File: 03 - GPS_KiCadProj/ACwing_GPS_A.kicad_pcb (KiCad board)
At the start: 2 copper layers, 30 x 30 mm, 28 parts, among them J1 Qwiic IN, J2 Qwiic OUT, Q1 2N7002, U1 SAM-M10Q-00B, U3 IIS2MDC

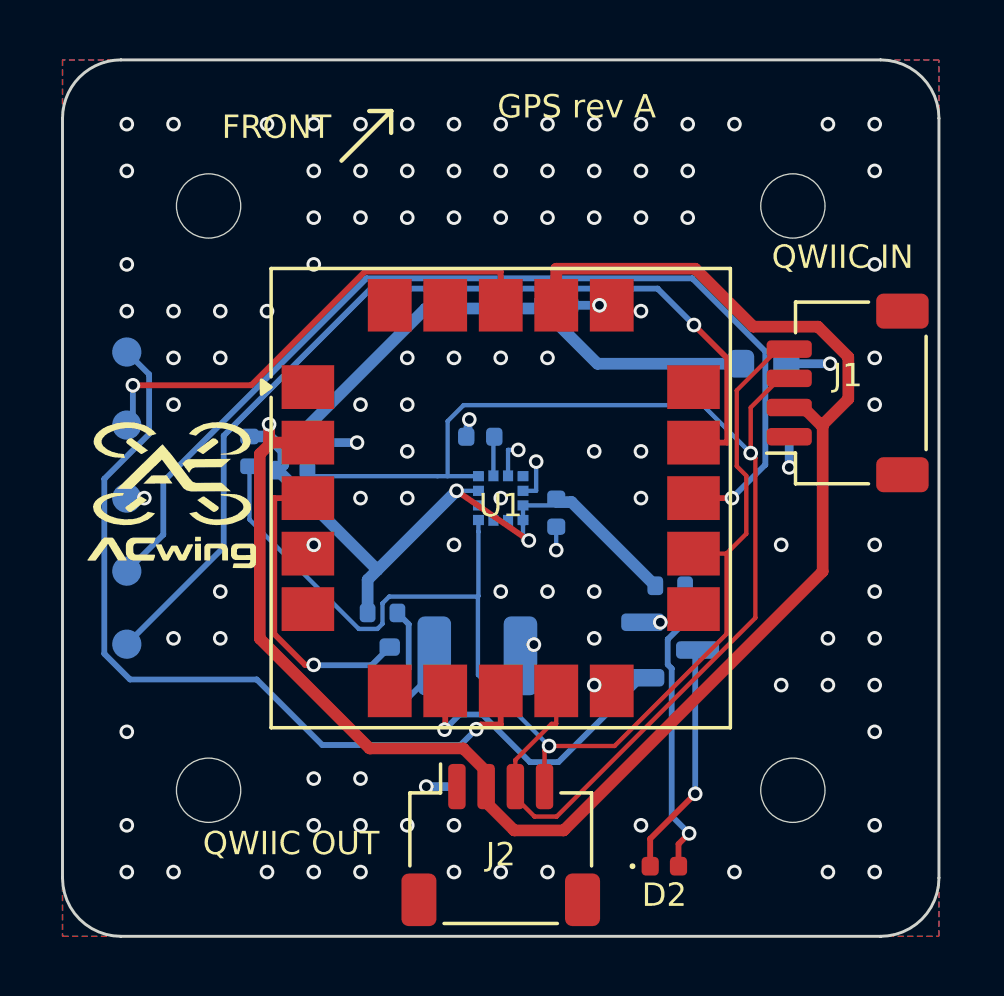
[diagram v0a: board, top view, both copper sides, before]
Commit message: Removed references of the passive components and of the ICs on the top and bottom silkscreen. Left only the labels of the connectors.
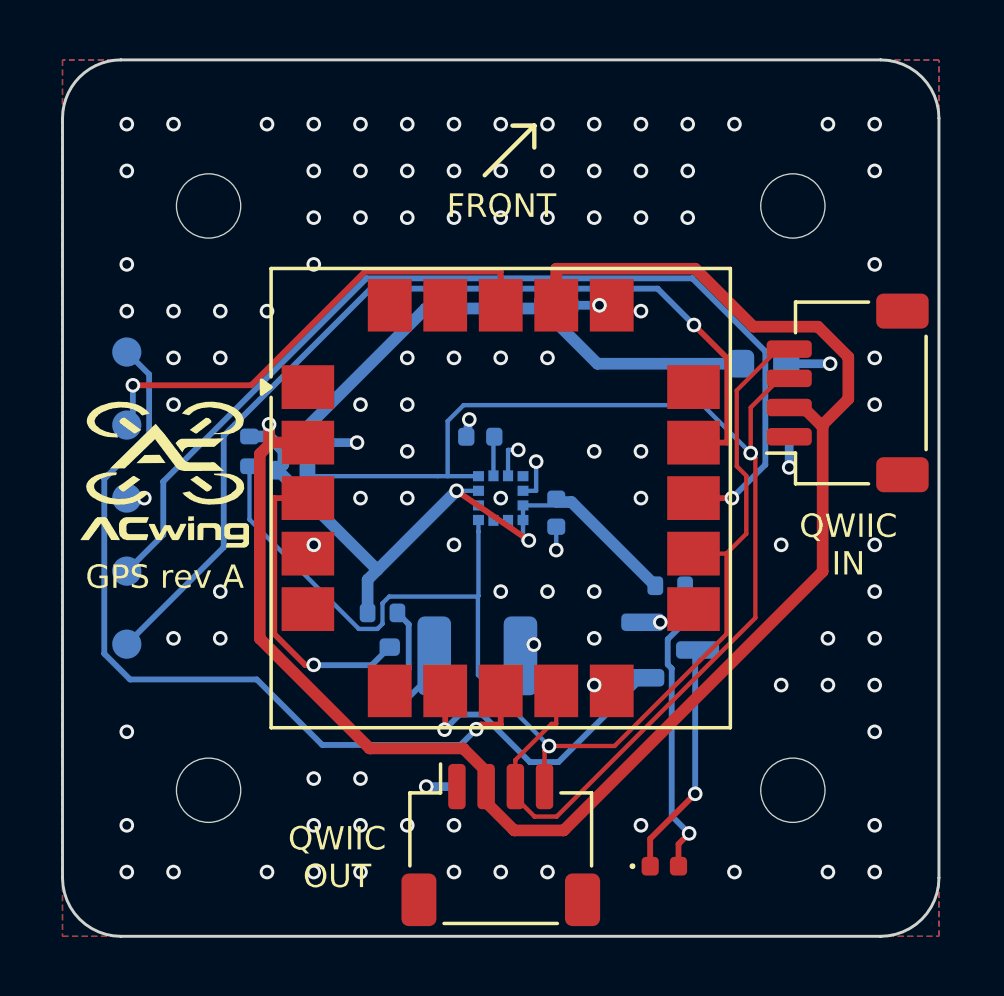
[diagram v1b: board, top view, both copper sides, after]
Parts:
- moved LOGO2 20.0 mm to (150.0, 90.5)
- moved LOGO1 0.74 mm to (138.5, 99.2)
